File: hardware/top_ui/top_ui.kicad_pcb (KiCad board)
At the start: 4 copper layers, 47 x 47 mm, 27 parts, among them J1 USB-C, J2 J_STK_A, J3 J_STK_B, J5 ST7789 240x280, J6 Stern Klinke, J7 Reserve UART, Q1 BC847, Q2 P-FET 20V 1A, SW1 BTN1, SW2 BTN2, SW3 BTN3, SW4 BTN4, U1 USBLC6-2SC6, U2 SHT40-AD1B, U3 VL53L1X

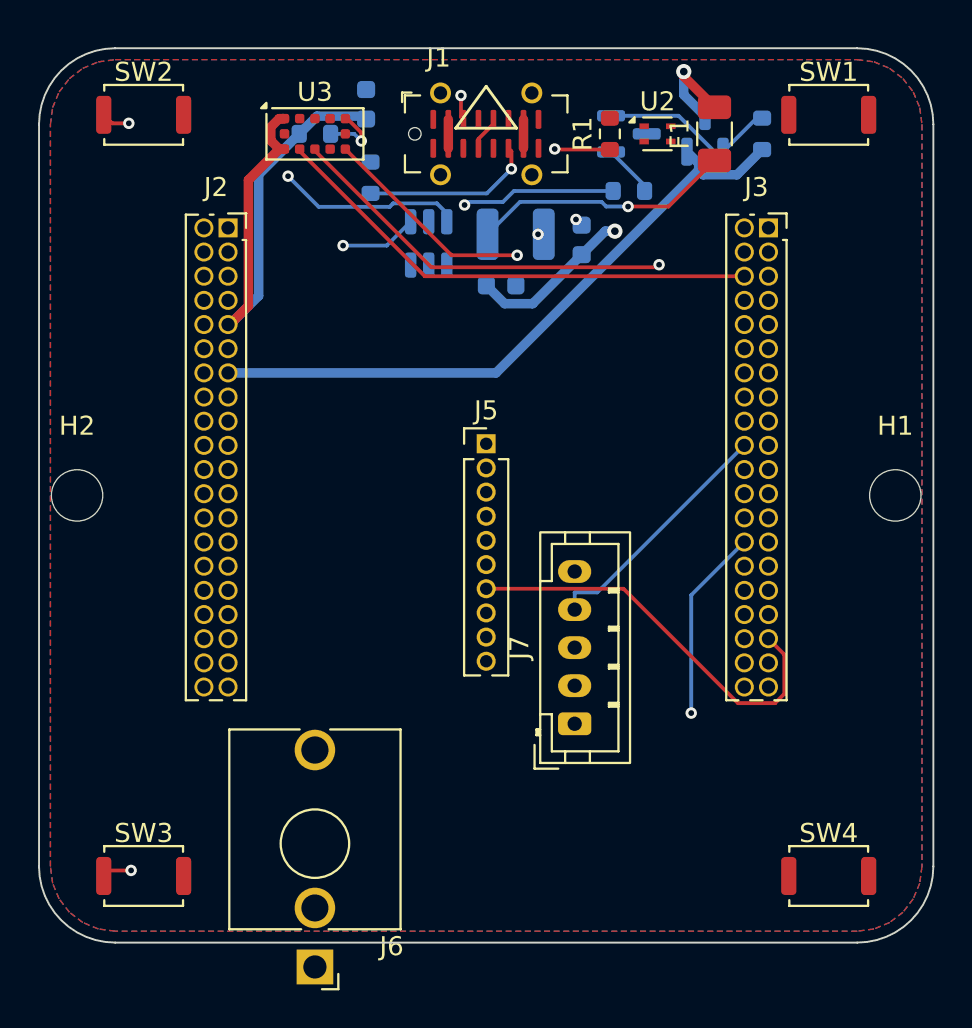
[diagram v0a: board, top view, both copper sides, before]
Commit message: USB-C wandert auf das Mid-Board, Top bekommt eine Randkerbe
Der Grund ist Bauhoehe, nicht Routing. Ueber dem Top-Board sind bis zur
Zentralscheibe 3,5 mm frei; eine stehende USB-C-Buchse baut 7 bis 9,25 mm
(GCT USB4115: H = 9,25 mm laut Datenblatt). Sie haette die Scheibe
durchstossen. Zwischen Mids und Tops Oberseite liegen dagegen 10,0 mm.

Die Buchse steht jetzt auf Mid bei (3,5 / 20,3) und greift durch eine offene
Randkerbe des Top-Boards nach vorn - gesteckt wird weiterhin frontal, sobald
die Zentralscheibe ab ist. Koerper 8,3 x 4,3 mm, Kerbe 11,0 mm breit ab
y = 16,8 bis zum Rand.

Offene Kerbe statt Fenster, weil der Boardrand bei y = 23,5 liegt: Ein
geschlossenes Fenster liesse einen Steg von einem halben Millimeter stehen,
der beim Nutzentrennen bricht.

MITGEWANDERT sind die ESD-Diode (U5) und die beiden CC-Widerstaende
(R18/R19). Damit verlieren USB_DP und USB_DN ihren Weg durch den Stapel:
J_STK_A 34/36 heissen jetzt RSV_A3/RSV_A5. Der native USB des ESP32-S3 sitzt
auf demselben Board wie die Buchse. Stack-Pinout auf v0.4.

USB_VBUS bleibt auf A18 - es geht weiter nach unten zum Power-Mux auf Bottom,
kommt jetzt nur von Mid statt von Top.

PLATZIERUNG. Der Bodenrand von Mid war belegt: RS485 (J4) nach links auf
(-11,5 / 19,0) gerueckt, PhotoMOS (U4) aus der Fixliste genommen. Ein
Rastersuchlauf ueber beide Seiten fand fuer U4 keine freie Flaeche von
11,6 x 3,6 mm - der automatische Platzierer bringt ihn jetzt selbst unter und
hat ihn nach (-20,1 / 7,9) gelegt. Oben ging es nicht, dort steht das
ESP32-Modul mit seiner Antenne; links und rechts laesst Tops Displayfenster
nur 7,2 mm Rand.

inside_outline() kennt die Kerbe, der Platzierer legt dort nichts ab, und der
Zonenumriss folgt ihr.

  top_ui     27 -> 21 Bauteile, unrouted 63 -> 48
  mid_logic  46 -> 50 Bauteile

Co-Authored-By: Claude Opus 5 (1M context) <noreply@anthropic.com>
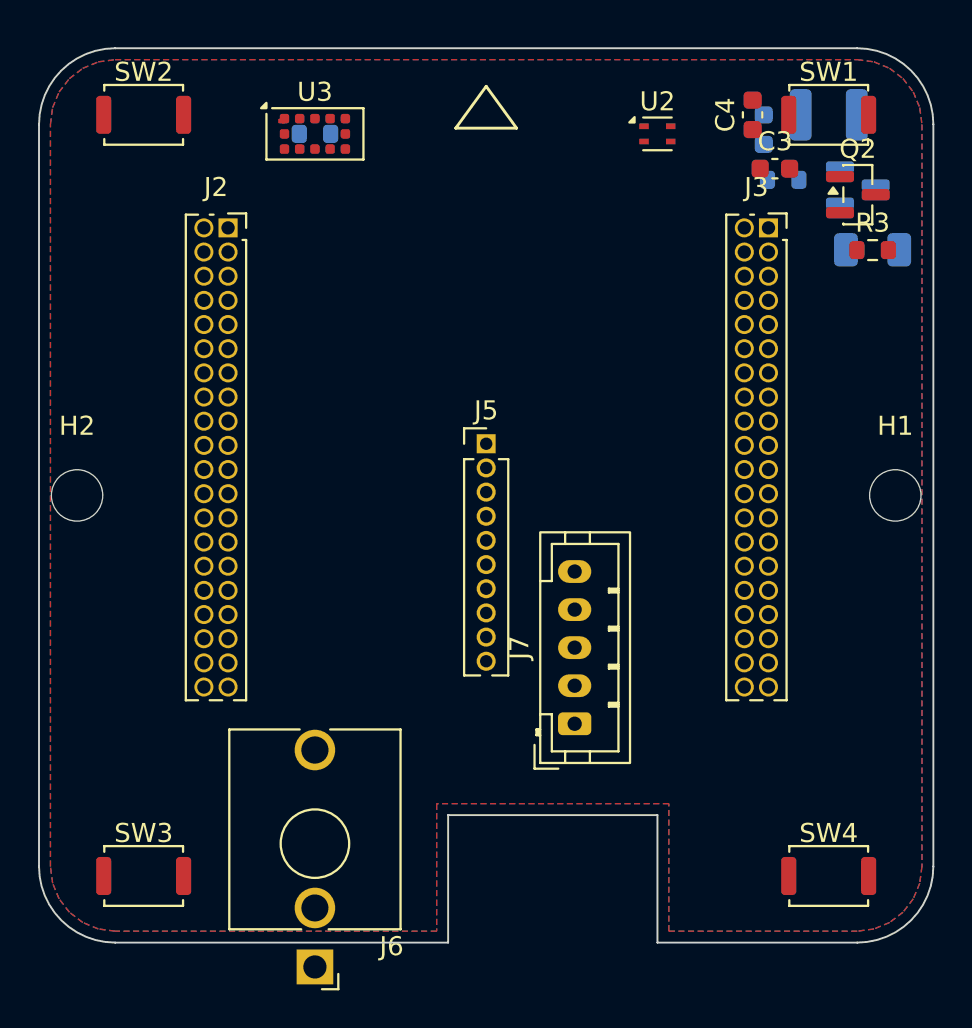
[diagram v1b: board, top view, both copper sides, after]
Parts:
- removed J1: USB-C, USB_C_Receptacle_G-Switch_GT-USB-7051x
- removed R1, R2: 5k1, R_0603_1608Metric
- removed U1: USBLC6-2SC6, SOT-23-6
- C3, C4, Q2, R3: moved to F.Cu
- F1: moved to B.Cu
- moved C1 20.9 mm to (14.6, -19.2)
- moved C2 17.6 mm to (18.0, -20.0)
- moved C4 16.0 mm to (14.0, -20.0), turned to 90 degrees
- moved R3 13.2 mm to (20.3, -12.9)
- moved Q1 12.3 mm to (19.5, -16.3)
- moved C3 10.8 mm to (15.2, -17.2), turned to 0 degrees
- moved F1 10.3 mm to (20.3, -12.9), turned to 0 degrees
- moved Q2 8.64 mm to (19.5, -15.8), turned to 0 degrees
- moved R4 2.66 mm to (15.6, -16.6), turned to 0 degrees
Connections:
- J2 pad 34: USB_DP -> RSV_A3
- J2 pad 36: USB_DN -> RSV_A5
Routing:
- net 3V3_SYS: track 96.8 -> 0.00 mm, vias 1 -> 0
- net PRESENCE_INT: track 56.6 -> 0.00 mm, vias 1 -> 0
- net BTN2: track 55.4 -> 0.00 mm, vias 1 -> 0
- net STAR_OUT: track 49.1 -> 0.00 mm, vias 1 -> 0
- net BTN3: track 44.6 -> 0.00 mm, vias 2 -> 0
- net USB_DN: track 39.0 -> 0.00 mm, vias 1 -> 0
- net 6V2_STAR_F: track 34.4 -> 0.00 mm
- net USB_DP: track 34.1 -> 0.00 mm, vias 1 -> 0
- net STAR_EN: track 28.4 -> 0.00 mm, vias 1 -> 0
- net QSPI_D0: track 27.9 -> 0.00 mm
- net I2C_SCL: track 26.2 -> 0.00 mm
- net I2C_SDA: track 26.0 -> 0.00 mm, vias 1 -> 0
- net QSPI_D3: track 21.6 -> 0.00 mm
- net DISP_RST: track 21.4 -> 0.00 mm
- net UART_AUX_TX: track 15.9 -> 0.00 mm
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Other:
- outline, holes or cut-outs redrawn

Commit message: Stack-Pinout v0.5: Tasten und I2C auf die Aussenreihe, Tasten auf beide Verbinder
Zwei Autorouter (1.9.0 und 2.3.0) und zwei Lagenzahlen hatten auf Top exakt
dieselben elf offenen Netze hinterlassen. Das ist kein Werkzeugproblem,
sondern die Pinbelegung.

BTN1..BTN4 lagen auf B26..B29 - vier benachbarten Kontakten der INNENreihe
des RECHTEN Verbinders. Ihre Taster sitzen aber in allen vier Ecken des
Top-Boards, zwei davon links. Zwei Bahnen mussten quer ueber ein Board mit
80 Steckkontakten im 1,27-mm-Raster, und alle vier zuerst aus der Innenreihe
heraus. I2C_SCL/SDA lagen ebenfalls innen.

Neu liegt jedes Tastennetz auf der AUSSENreihe des Verbinders, der seiner
Ecke am naechsten ist - von dort geht es direkt nach aussen und am Boardrand
entlang zum Taster:

  BTN1  B26 -> B1    aussen, y = -14,06   SW1 (+18 / -20)
  BTN2  B27 -> A2    aussen, y = -14,06   SW2 (-18 / -20)
  BTN3  B28 -> A40   aussen, y = +10,07   SW3 (-18 / +20)
  BTN4  B29 -> B39   aussen, y = +10,07   SW4 (+18 / +20)

  I2C_SCL  B6 -> B5  aussen
  I2C_SDA  B8 -> B7  aussen

Beide I2C-Teilnehmer auf Top - SHT4x und ToF - sitzen an der oberen Kante,
also dort, wo die neuen Pins liegen.

Die freigewordenen Kontakte B6, B8, B26..B29 werden PGND. Vier PGND-Pins sind
weggefallen (A2, A40, B1, B39); ueber beide Verbinder bleiben 25.

Alle drei Schaltplaene und Layouts neu erzeugt, Netzlistenvergleich bestanden,
keine Platzierungsfehler. Das Routing folgt.

Co-Authored-By: Claude Opus 5 (1M context) <noreply@anthropic.com>
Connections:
- J2 pad 2: PGND -> BTN2
- J2 pad 40: PGND -> BTN3
- J3 pad 1: PGND -> BTN1
- J3 pad 26: BTN1 -> PGND
- J3 pad 27: BTN2 -> PGND
- J3 pad 28: BTN3 -> PGND
- J3 pad 29: BTN4 -> PGND
- J3 pad 39: PGND -> BTN4
- J3 pad 5: PGND -> I2C_SCL
- J3 pad 6: I2C_SCL -> PGND
- J3 pad 7: PGND -> I2C_SDA
- J3 pad 8: I2C_SDA -> PGND

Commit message: Der Randkeepout war rund - auf dem quadratischen Top-Board eine Sperre
Damit ist erklaert, warum auf Top hartnaeckig dieselben elf Netze offen
blieben, egal was man aenderte.

route_boards.py legt dem Router einen Keepout an den Boardrand, weil KiCads
Specctra-Export den Kupfer-Randabstand nicht mitgibt. Dieser Keepout war ein
KREISRING von r = 25,6 bis 26,4 - ein Mass aus den runden Boards mit
Durchmesser 52.

Top ist aber ein Quadrat von 47 x 47, und seine vier Ecktaster sitzen bei
r = 26,91, also AUSSERHALB dieses Rings. Der Ring lag damit quer ueber die
Platine und trennte die Boardmitte von allen vier Tastern ab. Die
Tastennetze waren nie routbar:

  vier Lagen statt zwei      -> dieselben elf Netze
  Freerouting 2.3 statt 1.9  -> dieselben elf Netze
  Pinout v0.5, Aussenreihe   -> dieselben elf Netze

Drei Anlaeufe an derselben unsichtbaren Wand.

Das quadratische Board bekommt jetzt vier Balken entlang seiner Kanten
(SQ_RI = 23,0 bis SQ_RO = 25,0) statt eines Annulus. Der untere Balken hat
eine Luecke von x = -14 bis -4 fuer das absichtlich ueberstehende Pad der
Klinkenbuchse. Damit entfaellt auch der bisherige Winkel-Slit, der fuer die
USB-Buchse gedacht war - die sitzt seit heute auf Mid.

Die runden Boards bekommen unveraendert ihren Annulus.

Co-Authored-By: Claude Opus 5 (1M context) <noreply@anthropic.com>
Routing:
- net 3V3_SYS: track 0.00 -> 94.4 mm
- net PRESENCE_INT: track 0.00 -> 57.8 mm, vias 0 -> 1
- net 6V2_STAR_F: track 0.00 -> 45.5 mm, vias 0 -> 1
- net STAR_EN: track 0.00 -> 45.0 mm, vias 0 -> 1
- net I2C_SDA: track 0.00 -> 32.0 mm, vias 0 -> 1
- net I2C_SCL: track 0.00 -> 31.4 mm, vias 0 -> 1
- net QSPI_D0: track 0.00 -> 29.8 mm, vias 0 -> 1
- net QSPI_D3: track 0.00 -> 28.4 mm
- net DISP_RST: track 0.00 -> 21.4 mm
- net UART_AUX_RX: track 0.00 -> 20.0 mm
- net UART_AUX_TX: track 0.00 -> 15.9 mm
- net QSPI_D2: track 0.00 -> 15.1 mm
- net QSPI_D1: track 0.00 -> 14.7 mm
- net DISP_CS: track 0.00 -> 14.1 mm
- net DISP_BL: track 0.00 -> 13.7 mm
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
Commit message: Quadratischer Randkeepout: Top faellt von 11 auf 3 offene Netze
Der Kreisring war die Wand. Mit vier Balken entlang der Kanten statt eines
Annulus routet Freerouting auf Top durch:

              Segmente  Vias  offene Signale
  vorher         144      9        11
  jetzt          175     15         3   (3V3_SYS, I2C_SCL, I2C_SDA)

Alle vier Tastennetze und alle vier Stern-Netze sind jetzt verbunden. Damit
ist auch rueckwirkend klar, dass weder die Lagenzahl noch der Routerwechsel
noch das neue Pinout je eine Chance hatten - sie haben alle gegen dieselbe
unsichtbare Sperre gearbeitet.

DIE PROJEKTDATEIEN WERDEN BEIM SPEICHERN ZURUECKGESETZT. pcbnew.SaveBoard
legt die .kicad_pro mit KiCads Vorgaben neu an; die bewussten Entscheidungen
von gestern - 0,15 mm Abstand statt 0,2, ein Waermefallensteg statt zwei -
waren dadurch beim Neuerzeugen still verschwunden und erzeugten prompt wieder
Scheinverletzungen (Bottom 2 clearance, alle drei zusammen 34
starved_thermal). BoardBuilder.save() schreibt sie jetzt nach jedem Speichern
zurueck.

  starved_thermal  34 -> 0
  clearance         2 -> 1

STAND NACH gnd_connect

                Segmente  offene Signale  Masse-Inseln  Kupferfehler
  top_ui           175          3              1             1
  mid_logic        641          9             12             0
  bottom_power    1430          4             26             1

Der eine Kupferfehler auf Top ist der dokumentierte, absichtliche Ueberhang
der Klinkenbuchse ueber die Boardkante; der auf Bottom ein Haarriss von
0,1 statt 0,15 mm zwischen zwei Leistungsbahnen.

Co-Authored-By: Claude Opus 5 (1M context) <noreply@anthropic.com>
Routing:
- net STAR_OUT: track 0.00 -> 54.1 mm, vias 0 -> 1
- net STAR_SW: track 0.00 -> 15.0 mm, vias 0 -> 2
- net BTN3: track 0.00 -> 12.1 mm
- net BTN1: track 0.00 -> 11.1 mm, vias 0 -> 1
- net BTN4: track 0.00 -> 10.4 mm
- net PRESENCE_INT: track 57.8 -> 67.2 mm
- net BTN2: track 0.00 -> 8.12 mm
- net 6V2_STAR_F: track 45.5 -> 37.9 mm, vias 1 -> 2
- net UART_AUX_RX: track 20.0 -> 13.0 mm
- net STAR_EN: track 45.0 -> 50.5 mm, vias 1 -> 2
- net I2C_SDA: track 32.0 -> 32.9 mm
- net STAR_G: track 5.32 -> 5.92 mm
- net I2C_SCL: track 31.4 -> 30.9 mm
- net PGND: vias 0 -> 1

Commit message: Der Original-Controller bestaetigt die Strommessung ein viertes Mal
Der mitgelieferte K0000230 lag offen auf dem Tisch. Drei Bauteile darauf
sagen dasselbe wie unsere drei Messungen - und man muss dafuer nichts messen:

  Shunt 50 mOhm je Kanal   bei 1,7 A sind das 85 mV und 0,14 W.
                           Bei 20 A waeren es 20 WATT in einem Chipwiderstand.
  2x Infineon BTM7700G     integrierte H-Bruecke, rund 110 mOhm im Strompfad.
                           Bei 1,7 A 0,32 W, bei 20 A 44 W in einem SO-28.
  Elko 47 uF               fuer zwei Motoren. Wer 20-A-Impulse abfaengt,
                           baut Hunderte von Mikrofarad ein.

Drei unabhaengige Bauteilentscheidungen, alle nur mit ein bis zwei Ampere
vereinbar. docs/14 neu, mit der vollstaendigen Bauteilliste.

DREI FOLGERUNGEN FUER UNS

1) Unsere diskrete Bruecke aus acht MOSFETs und vier Gate-Treibern loest der
   Hersteller mit ZWEI ICs. Das war Punkt 55; das Argument dagegen (Platine
   ist geroutet) steht weiter, aber die Sachlage ist jetzt belegt statt
   vermutet. Der BTM7700G selbst waere fuer uns grenzwertig - seine
   Kurzschlussfestigkeit endet bei 28 V, unsere Schiene liegt bei 26,4 V.

2) Der Bulk-Kondensator darf schrumpfen. docs/01 sieht 470 bis 1000 uF vor,
   das Original kommt mit 47 uF aus. Das ist die praktisch wertvollste
   Erkenntnis, denn der Elko ist eines der groessten Teile auf der Kabelseite
   von Bottom - genau dort, wo heute der Platz fuer einen zusammengefassten
   Feldstecker fehlt. Nicht blind uebernehmen: 100 bis 220 uF sind die
   naheliegende Groessenordnung fuer unsere PWM-Topologie.

3) Der Hersteller trennt seine Eingaenge galvanisch (zwei Optokoppler), wir
   nicht. Bei reiner SELV-Verkabelung zulaessig, aber ein Konzeptunterschied.

Ausserdem in diesem Commit:

  3D-Modelle fuer die drei Steckverbinder, die KiCad nicht mitliefert
  (mechanical/connector_models.py) - Huellkoerper aus dem F.Fab-Grundriss,
  Hoehen mit Quelle dokumentiert. gen_layouts haengt sie 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
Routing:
- net STAR_G: track 5.92 -> 14.6 mm
- net STAR_EN: track 50.5 -> 44.8 mm, vias 2 -> 1
- net PRESENCE_INT: track 67.2 -> 62.2 mm, vias 1 -> 2
- net BTN1: track 11.1 -> 6.38 mm, vias 1 -> 0
- net STAR_SW: track 15.0 -> 10.6 mm, vias 2 -> 0
- net 3V3_SYS: track 94.5 -> 92.3 mm
- net I2C_SDA: track 32.9 -> 34.8 mm
- net PGND: track 0.00 -> 1.50 mm
- net 6V2_STAR_F: track 37.9 -> 39.1 mm, vias 2 -> 1

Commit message: docs/16: Anleitung fuer die letzten Handgriffe in KiCad
Was der Autorouter uebrig laesst, ist wenig und immer dasselbe Muster: Pads,
die zwischen anderen Bauteilen eingeklemmt sind. Die Anleitung nennt die
Tastenkuerzel (X fuer Bahn, V fuer Lagenwechsel mit Via, B fuer Zonen
fuellen), den aktuellen Stand je Board als Anhaltspunkt und die
Reihenfolge danach - Zonen fuellen VOR der DRC, sonst sucht man Fehler, die
keine sind.

Dazu zwei Warnungen: keine Bauteile verschieben, die Positionen kommen aus
gen_layouts.py und gehen beim naechsten Neuerzeugen verloren. Und die Regeln
nicht lockern - wenn die DRC meckert, ist die Bahn falsch.

Co-Authored-By: Claude Opus 5 (1M context) <noreply@anthropic.com>
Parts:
- removed J7: Reserve UART, JST_PH_B5B-PH-K_1x05_P2.00mm_Vertical
- moved J6 9.00 mm to (0.00, 24.8)
- moved R5 5.50 mm to (-3.50, -19.0)
- moved U2 5.50 mm to (3.50, -19.0)
- moved U3 5.50 mm to (-3.50, -19.0)
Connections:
- net RSV_A2 renamed REED2_IN
- net RSV_A3 renamed RS485_A
- net RSV_A4 renamed RS485_B
- net RSV_A5 renamed REED1_IN
- net RSV_A6 renamed SAB1_IN
- J2 pad 25: PGND -> SAB2_IN
- J2 pad 38: PGND -> HOOD_A
- J2 pad 39: PGND -> HOOD_B
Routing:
- net PRESENCE_INT: track 62.2 -> 37.1 mm, vias 2 -> 1
- net UART_AUX_TX: track 15.8 -> 0.00 mm
- net UART_AUX_RX: track 13.0 -> 0.00 mm
- net 3V3_SYS: track 92.3 -> 80.2 mm
- net STAR_G: track 14.6 -> 5.51 mm
- net BTN1: track 6.38 -> 13.6 mm, vias 0 -> 1
- net I2C_SDA: track 34.8 -> 28.2 mm
- net I2C_SCL: track 30.4 -> 25.9 mm
- net STAR_OUT: track 54.6 -> 50.7 mm
- net STAR_EN: track 44.8 -> 40.9 mm, vias 1 -> 2
- net STAR_SW: track 10.6 -> 8.70 mm
- net PGND: track 1.50 -> 0.00 mm, vias 1 -> 0
- net QSPI_D3: track 28.0 -> 26.5 mm
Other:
- outline, holes or cut-outs redrawn

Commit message: docs/17: woher die Daten der vier offenen Bauteile kommen
Display, Klinkenbuchse, USB-C und Feldstecker blockieren die Bestellung -
jedes aus einem anderen Grund. Die Seite sagt je Teil, was genau fehlt, wo es
herkommt und was davon abhaengt.

DISPLAY ist der kritische Fall: Im Schaltplan steht ein Platzhalter, ein
1,27-mm-Stiftleisten-Footprint mit zehn Pins und dem Vermerk PLATZHALTER. Es
ist weder ein Bauteil gewaehlt noch ein Anschluss festgelegt.

Dabei faellt eine Bauform schon raus: Die verbreiteten Fertigmodule mit
Traegerplatine messen 48 x 31 mm - einen Millimeter breiter als unser
Top-Board. Es muss ein nacktes Panel mit FPC-Fahne sein, rund 30 x 36 mm.
Kandidaten bei buydisplay.com (ER-TFT1.69-1), Datenblaetter dort nur im
Browser, automatische Downloads blockt der Anbieter.

Fuenf Zahlen sind aus dem Datenblatt zu holen, und eine davon ist die
entscheidende: die Lage der AKTIVEN Flaeche im Aussenmass. Das Fenster der
Zentralscheibe misst 32,7 x 27,0 und liegt bei (-0,95 / +0,3) - ein Panel mit
asymmetrischem Rand verschiebt das Bild darin.

SCHRAUBKLEMMEN STATT STECKVERBINDER geprueft und verworfen. Sie sind
einreihig, sechzehn Pole werden dadurch doppelt so lang:

  Schraubklemme 3,5 mm   56,0 mm   passt nicht auf Durchmesser 52
  Schraubklemme 2,54 mm  40,6 mm   passt, aber winzig
  Micro-Fit 3.0 2x8      28,15 mm  passt

Dazu entfiele der vorbereitete Kabelbaum mit einem Klick - bei Schraubklemmen
wird in der Dose geschraubt, einzeln, ueber Kopf. Empfehlung: Micro-Fit
behalten, das STEP-Modell gibt es bei Molex zu jeder Bestellnummer.

Co-Authored-By: Claude Opus 5 (1M context) <noreply@anthropic.com>
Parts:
- C4: moved to B.Cu
- moved J6 9.00 mm to (-9.00, 24.8)
- moved R5 9.00 mm to (5.50, -19.0)
- moved U2 9.00 mm to (12.5, -19.0)
- moved U3 9.00 mm to (5.50, -19.0)
- moved C3 4.78 mm to (13.2, -21.5)
- moved C4 2.01 mm to (12.7, -18.5)
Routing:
- net 3V3_SYS: track 80.2 -> 0.00 mm
- net STAR_OUT: track 50.7 -> 0.00 mm, vias 1 -> 0
- net STAR_EN: track 40.9 -> 0.00 mm, vias 2 -> 0
- net 6V2_STAR_F: track 38.7 -> 0.00 mm, vias 1 -> 0
- net PRESENCE_INT: track 37.1 -> 0.00 mm, vias 1 -> 0
- net QSPI_D0: track 29.9 -> 0.00 mm, vias 1 -> 0
- net I2C_SDA: track 28.2 -> 0.00 mm, vias 1 -> 0
- net QSPI_D3: track 26.5 -> 0.00 mm
- net I2C_SCL: track 25.9 -> 0.00 mm, vias 1 -> 0
- net DISP_RST: track 21.1 -> 0.00 mm
- net QSPI_D2: track 14.7 -> 0.00 mm
- net QSPI_D1: track 14.7 -> 0.00 mm
- net DISP_CS: track 14.1 -> 0.00 mm
- net BTN1: track 13.6 -> 0.00 mm, vias 1 -> 0
- net DISP_BL: track 13.6 -> 0.00 mm
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
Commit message: Display gewaehlt: ER-TFT1.69-3, 12-polige FPC steckbar
  aktive Flaeche   27,97 x 32,63 mm
  sichtbar         28,97 x 33,63 mm
  Aussenmass       30,07 x 37,43 x 1,6 mm (FPC gefaltet)
  Treiber          ST7789V, 4-Draht-SPI

Quer eingebaut misst die aktive Flaeche 32,63 x 27,97 gegen ein Fenster von
32,70 x 27,00 - in der Breite bleiben 0,07 mm Luft, in der Hoehe verdeckt die
Zentralscheibe oben und unten je 0,49 mm. Rund acht Pixel je Seite, bewusst in
Kauf genommen. Die Firmware darf in diesen Zeilen nichts Wichtiges zeichnen.

Auf dem Top-Board passt es: 1,6 mm Dicke gegen 2,0 mm Budget, und in y reicht
das Panel nur bis +/-15,04 und bleibt damit frei von den Ecktastern bei
18,27..21,73. In x reicht es bis +/-18,71 und liegt NEBEN den Tastern, mit rund
1,5 mm diagonalem Abstand - das ist am realen Teil anzusehen.

J5 steht damit nicht mehr auf einem erfundenen 1,27-mm-Stiftleisten-Footprint
mit zehn Polen, sondern auf zwoelf Polen mit FPC-Buchse.

ZWEI ZAHLEN FEHLEN WEITERHIN, beide nur aus dem Datenblatt zu holen:

  Das RASTER der Fahne. Die Loetvariante ist mit 0,7 mm angegeben, und KiCad
  bringt fuer 0,7 mm kein einziges FPC-Footprint mit - nur 0,5 und 1,0. Ist es
  wirklich 0,7, muss eines in die Projektbibliothek gezeichnet werden. Bis
  dahin steht ein 0,5-mm-Footprint mit der richtigen Polzahl.

  Die PINBELEGUNG. Zwoelf Pole sind gesichert, welches Signal auf welchem
  liegt nicht. Die Zuordnung im Schaltplan ist die des alten Platzhalters und
  mit hoher Wahrscheinlichkeit falsch.

Beides steht so im Schaltplan-Generator, damit es niemand uebersieht: Solange
es offen ist, darf das Top-Board nicht bestellt werden.

Co-Authored-By: Claude Opus 5 (1M context) <noreply@anthropic.com>
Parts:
- J5: value ST7789 240x280 -> ER-TFT1.69-3; footprint PinHeader_1x10_P1.27mm_Vertical -> TE_1-1734839-2_1x12-1MP_P0.5mm_Horizontal
- moved J5 4.79 mm to (0.00, 2.08)
